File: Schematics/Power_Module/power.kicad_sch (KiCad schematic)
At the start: 77 parts, among them J2 ScrewSwitch, J3 Battery, J6 ScrewSwitch, J7 GSE, Q1 AO4447A, Q2 AO4447A, Q3 AO3400A, Q4 AO3400A, U1 LMR51430XDDCR, U10 TPS61175PWPR, U14 LM74700QDBVRQ1, U15 LM74700QDBVRQ1, U2 LMR51430XDDCR, U3 ACS37041KLHBLT-010B3, U4 AMS1117-3.3, U5 ACS37041KLHBLT-010B3, U6 LM66100DCKR, U7 LM66100DCKR, U8 LM66100DCKR

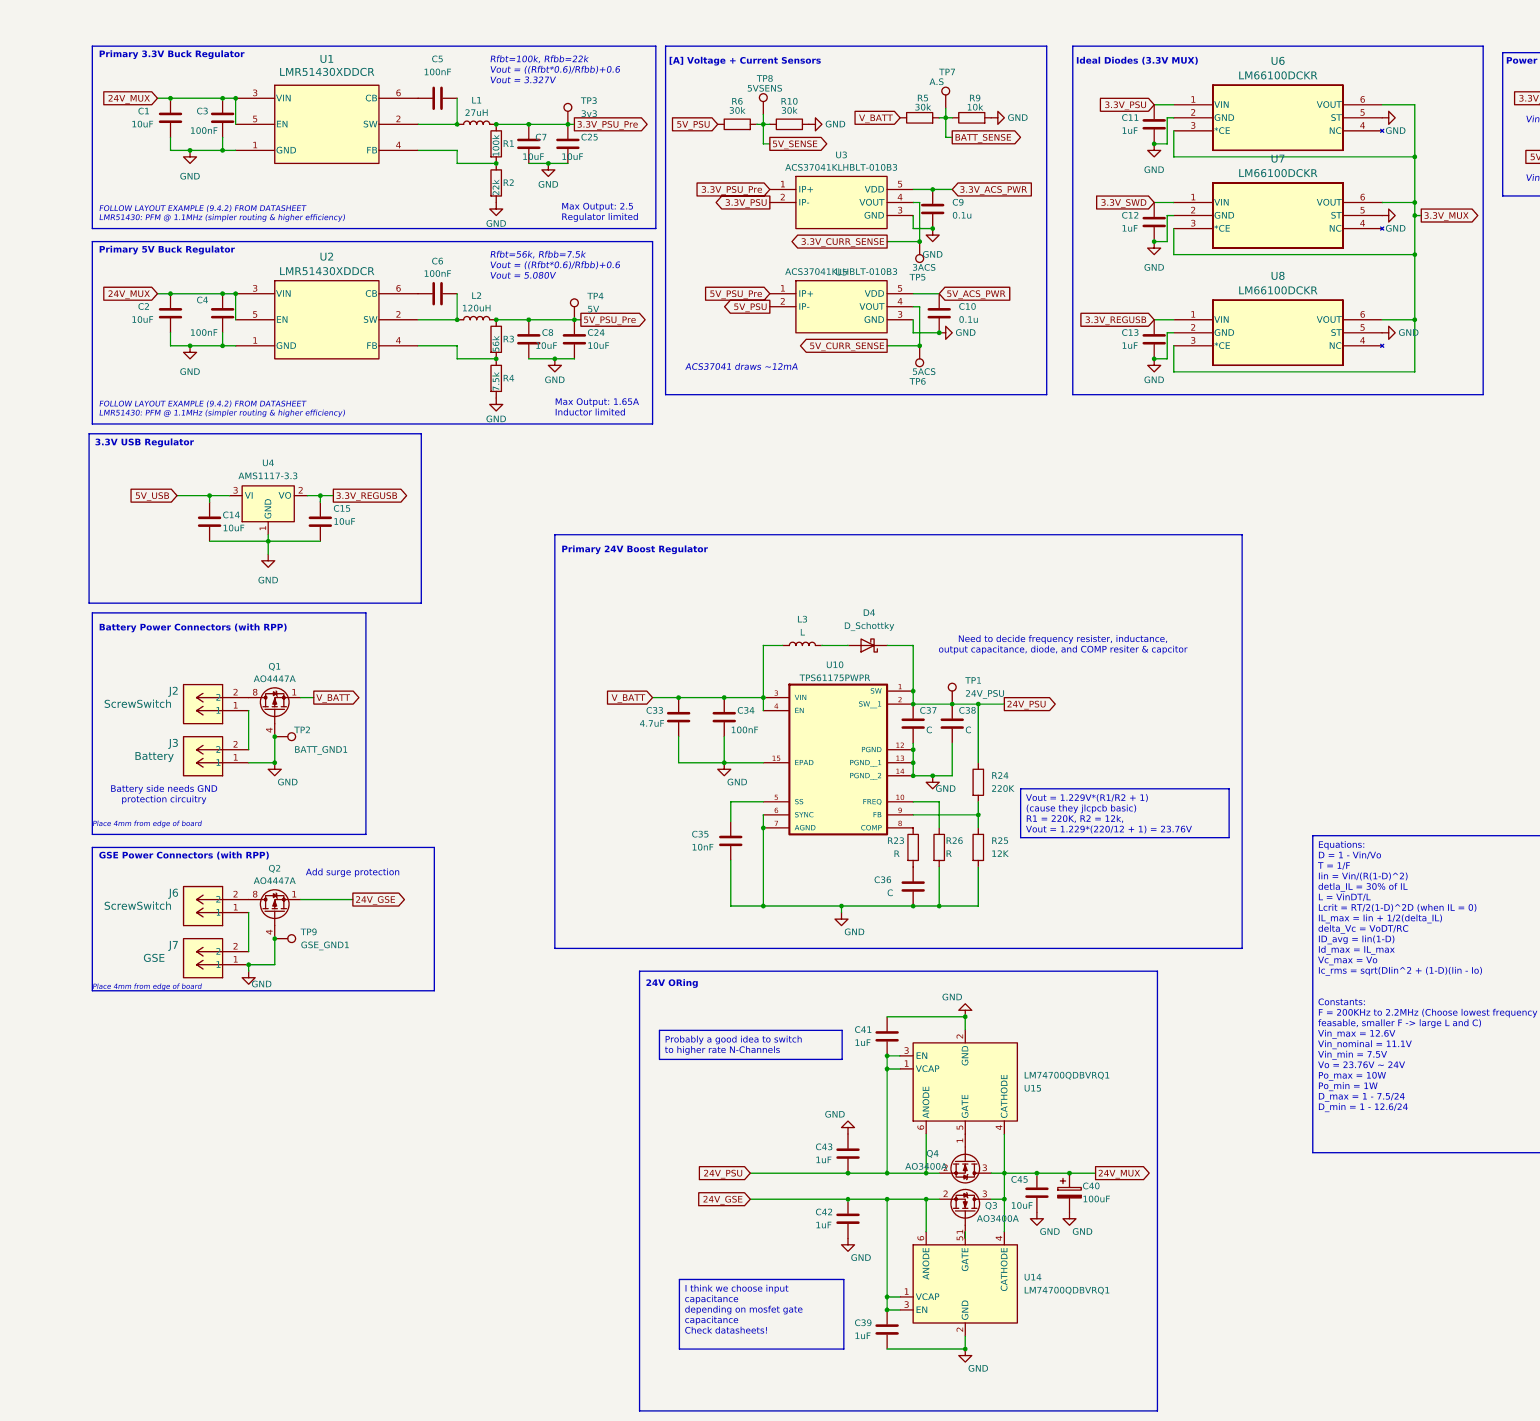
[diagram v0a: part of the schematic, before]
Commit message: complete clamping and rpp for 24v gse source  - chose 24v source ORing mosfet
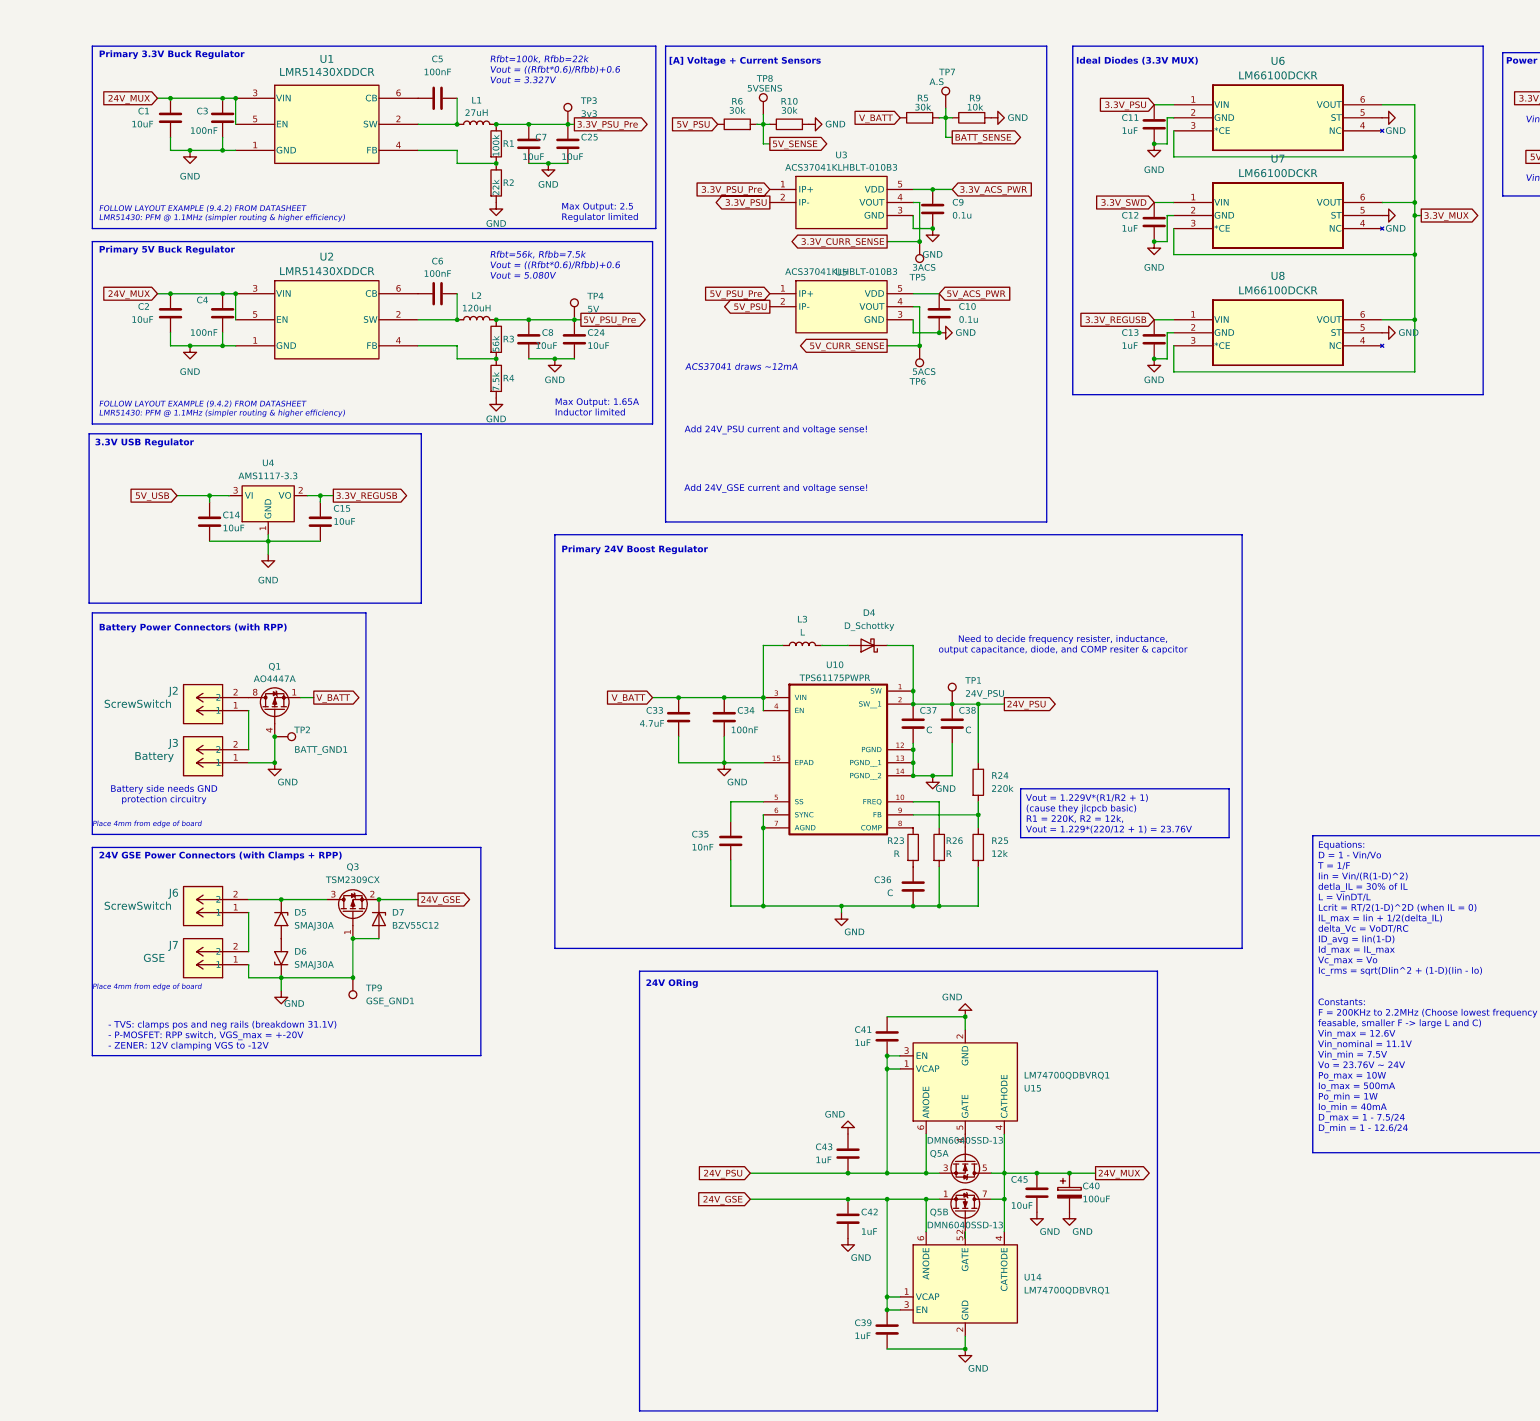
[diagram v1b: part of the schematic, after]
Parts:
- removed Q2: AO4447A, Package_SO:SOIC-8_3.9x4.9mm_P1.27mm, symbol Transistor_FET:IRF7404
- removed Q3, Q4: AO3400A, Package_TO_SOT_SMD:SOT-23, symbol Transistor_FET:AO3400A
- added D5, D6: SMAJ30A, Diode_SMD:D_SMA, symbol Diode:SMAJ30A
- added D7: BZV55C12, Diode_SMD:D_MiniMELF, symbol Diode:BZV55C12
- added Q3: TSM2309CX, Package_TO_SOT_SMD:SOT-23, symbol Transistor_FET:TSM2301ACX
- added Q5: DMN6040SSD-13, Package_SO:SOIC-8_3.9x4.9mm_P1.27mm, symbol Transistor_FET:STS2DNE60
- C35: footprint Capacitor_SMD:C_0805_2012Metric -> Capacitor_SMD:C_0603_1608Metric
- R24: value 220K -> 220k; footprint (none) -> Resistor_SMD:R_0603_1608Metric
- R25: value 12K -> 12k; footprint (none) -> Resistor_SMD:R_0603_1608Metric
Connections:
- net 24V_GSE: now also D7.1 (K), Q3.2 (S), Q5.1 (S1)
- net 24V_MUX: now also Q5.5 (D2), Q5.6 (D2), Q5.7 (D1), Q5.8 (D1)
- net 24V_PSU: now also Q5.3 (S2)
- net GND: now also D6.1 (A1), D7.2 (A), Q3.1 (G)
- net at U15.5 (GATE): now also Q5.4 (G2)
- net at U14.5 (GATE): now also Q5.2 (G1)
- net at J6.2: now also D5.1 (A1), Q3.3 (D)
- new net: D5.2 (A2), D6.2 (A2)
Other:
- note added: "- TVS: clamps pos and neg rails (breakdown 31.1V) - P-MOSFET: RPP switch, VGS_max = +-20V - ZENER: 12V clamping VGS to -12V"
- note added: "24V GSE Power Connectors (with Clamps + RPP)"
- note added: "Add 24V_GSE current and voltage sense!"
- note added: "Add 24V_PSU current and voltage sense!"
- note removed: "Add surge protection"
- note removed: "GSE Power Connectors (with RPP)"
- moved on the sheet: TP9

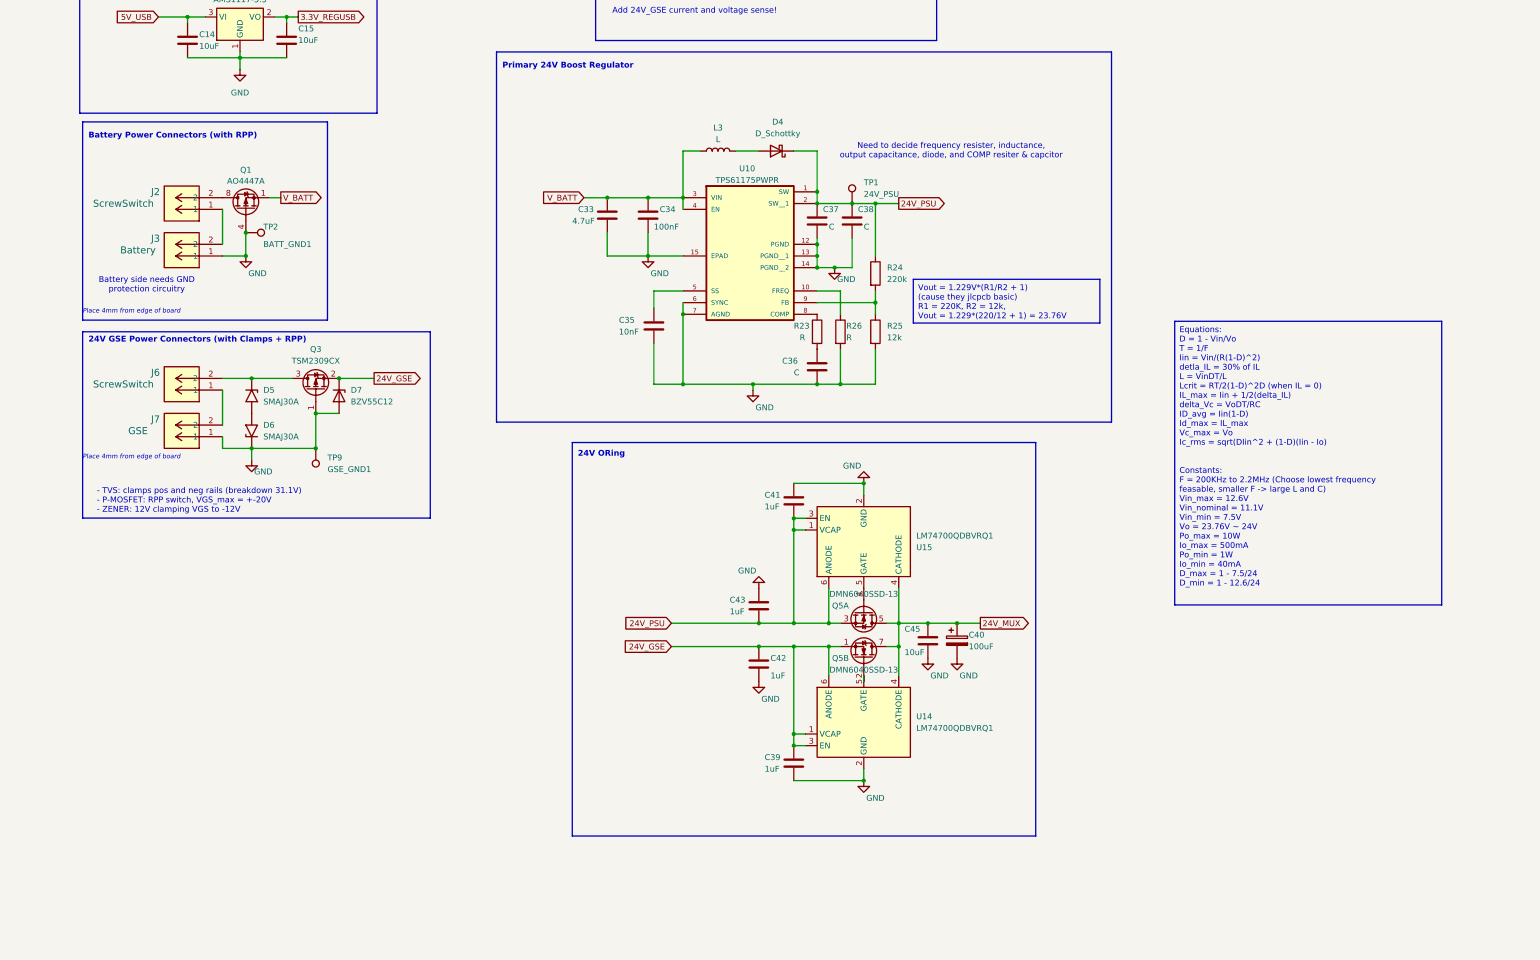
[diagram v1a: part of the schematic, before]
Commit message: ongoing equation for boost calculations
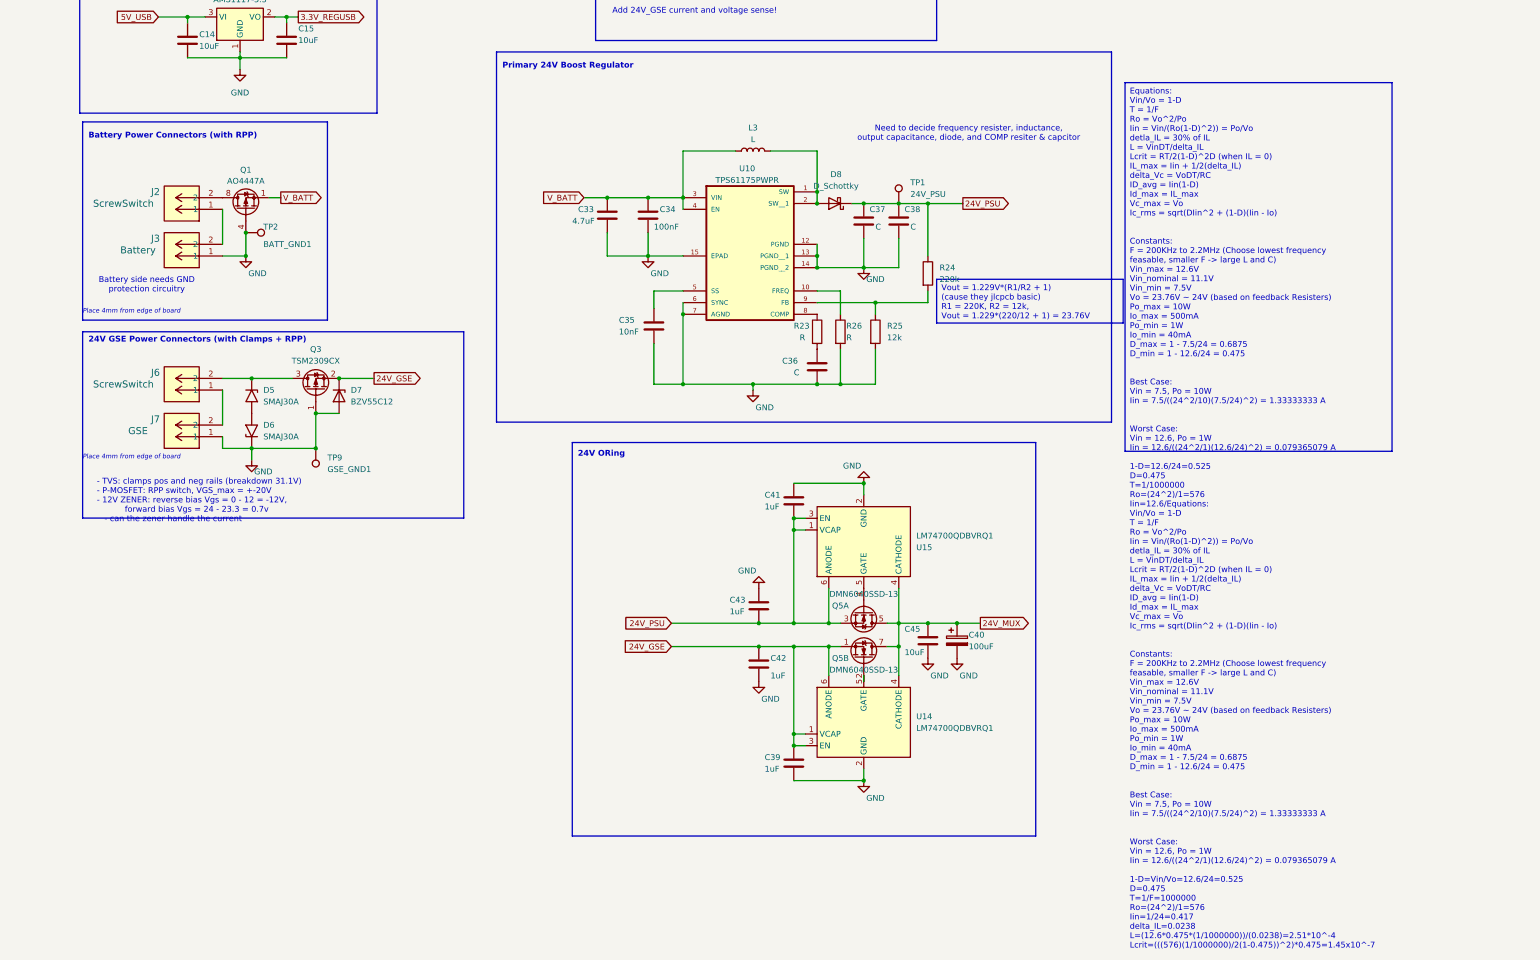
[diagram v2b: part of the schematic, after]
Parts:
- removed D4: D_Schottky, symbol Device:D_Schottky
- added D8: D_Schottky, symbol Device:D_Schottky
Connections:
- net 24V_PSU: now also D8.1 (K); no longer U10.1 (SW), U10.2 (SW__1)
- net at L3.2: now also U10.1 (SW), U10.2 (SW__1), D8.2 (A)
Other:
- note added: "- TVS: clamps pos and neg rails (breakdown 31.1V) - P-MOSFET: RPP switch, VGS_max = +-20V - 12V ZENER: reverse bias Vgs = 0 - 12 = -12V, forward bias Vgs = 24 - 23.3 = 0.7v - can the zener handle the current"
- note removed: "- TVS: clamps pos and neg rails (breakdown 31.1V) - P-MOSFET: RPP switch, VGS_max = +-20V - ZENER: 12V clamping VGS to -12V"
- moved on the sheet: C38, L3, R24, TP1

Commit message: Update power.kicad_sch
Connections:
- net 24V_MUX: now also Q5.7 (D1), Q5.8 (D1); no longer Q5.5 (D2), Q5.6 (D2)
- net 24V_PSU: now also Q5.1 (S1); no longer Q5.3 (S2)
- net at U15.5 (GATE): now also Q5.2 (G1); no longer Q5.4 (G2)

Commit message: Reverted Commit
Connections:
- net 24V_MUX: now also Q5.5 (D2), Q5.6 (D2); no longer Q5.7 (D1), Q5.8 (D1)
- net 24V_PSU: now also Q5.3 (S2); no longer Q5.1 (S1)
- net at U15.5 (GATE): now also Q5.4 (G2); no longer Q5.2 (G1)
